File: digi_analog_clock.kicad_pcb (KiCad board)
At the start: 2 copper layers, 172 parts, among them SW1 SW_Push, SW2 SW_Push, U1 ATtiny13A-SSU, U2 MCP7940N-xSN, Y1 7pF CL

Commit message: Some updates, not finished
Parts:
- added J1: USB_B_Micro, digikey-footprints:USB_Micro_B_Female_10118194-0001LF, B.Cu at (100.0, 145.0)
- BT1, C1, C2, R3: moved to B.Cu
- moved D49 148.3 mm to (62.9, 87.9), turned to 162 degrees
- moved D50 143.9 mm to (64.4, 84.1), turned to 156 degrees
- moved D51 143.5 mm to (66.2, 80.5), turned to 150 degrees
- moved C13 137.7 mm to (65.8, 88.9), turned to 252 degrees
- moved D52 137.0 mm to (68.4, 77.1), turned to 144 degrees
- moved D53 135.9 mm to (71.0, 73.9), turned to 138 degrees
- moved D54 129.0 mm to (73.9, 71.0), turned to 132 degrees
- moved D129 126.9 mm to (61.0, 122.5), turned to 210 degrees
- moved D130 122.2 mm to (55.0, 100.0), turned to 180 degrees
- moved D96 122.1 mm to (83.5, 128.6), turned to 240 degrees
- moved D36 120.4 mm to (80.5, 133.8), turned to 240 degrees
- moved D95 117.2 mm to (86.6, 130.1), turned to 246 degrees
- moved D131 116.4 mm to (61.0, 77.5), turned to 150 degrees
- moved D128 116.1 mm to (77.5, 139.0), turned to 240 degrees
- moved D93 114.8 mm to (93.1, 132.3), turned to 258 degrees
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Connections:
- net /sheet5E4278E1/DIN renamed /6x_sk6805_1515_hours_1/DIN
- net /sheet5E4278E2/DIN renamed /6x_sk6805_1515_hours_2/DIN
- D1 pad 3: /6x_sk6805_1515_mins_2/DIN -> /6x_sk6805_1515_mins_1/DIN
- D12 pad 1: /6x_sk6805_1515_mins_4/DIN -> /6x_sk6805_1515_mins_3/DIN
- D13 pad 3: /6x_sk6805_1515_mins_4/DIN -> /6x_sk6805_1515_mins_3/DIN
- D132 pad 1: /sheet5E4278E2/DOUT -> (no net)
- D18 pad 1: /6x_sk6805_1515_mins_5/DIN -> /6x_sk6805_1515_mins_4/DIN
- D19 pad 3: /6x_sk6805_1515_mins_5/DIN -> /6x_sk6805_1515_mins_4/DIN
- D24 pad 1: /6x_sk6805_1515_mins_6/DIN -> /6x_sk6805_1515_mins_5/DIN
- D25 pad 3: /6x_sk6805_1515_mins_1/DIN -> /6x_sk6805_1515_mins_5/DIN
- D30 pad 1: /6x_sk6805_1515_mins_2/DIN -> /6x_sk6805_1515_mins_6/DIN
- D6 pad 1: /6x_sk6805_1515_mins_3/DIN -> /6x_sk6805_1515_mins_2/DIN
- D61 pad 3: /6x_sk6805_1515_secs_2/DIN -> /6x_sk6805_1515_secs_1/DIN
- D66 pad 1: /6x_sk6805_1515_secs_3/DIN -> /6x_sk6805_1515_secs_2/DIN
- D67 pad 3: /6x_sk6805_1515_secs_3/DIN -> /6x_sk6805_1515_secs_2/DIN
- D7 pad 3: /6x_sk6805_1515_mins_3/DIN -> /6x_sk6805_1515_mins_2/DIN
- D72 pad 1: /6x_sk6805_1515_secs_4/DIN -> /6x_sk6805_1515_secs_3/DIN
- D73 pad 3: /6x_sk6805_1515_secs_4/DIN -> /6x_sk6805_1515_secs_3/DIN
- D78 pad 1: /6x_sk6805_1515_secs_5/DIN -> /6x_sk6805_1515_secs_4/DIN
- D79 pad 3: /6x_sk6805_1515_secs_5/DIN -> /6x_sk6805_1515_secs_4/DIN
- D84 pad 1: /6x_sk6805_1515_secs_6/DIN -> /6x_sk6805_1515_secs_5/DIN
- D85 pad 3: /6x_sk6805_1515_secs_1/DIN -> /6x_sk6805_1515_secs_5/DIN
- D90 pad 1: /6x_sk6805_1515_secs_2/DIN -> /6x_sk6805_1515_secs_6/DIN
- U2 pad 7: Net-(U2-Pad7) -> (no net)
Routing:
- added copper zone on B.Cu, net GND
- added copper zone on F.Cu, net GND
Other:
- board outline added: 98 x 98 mm

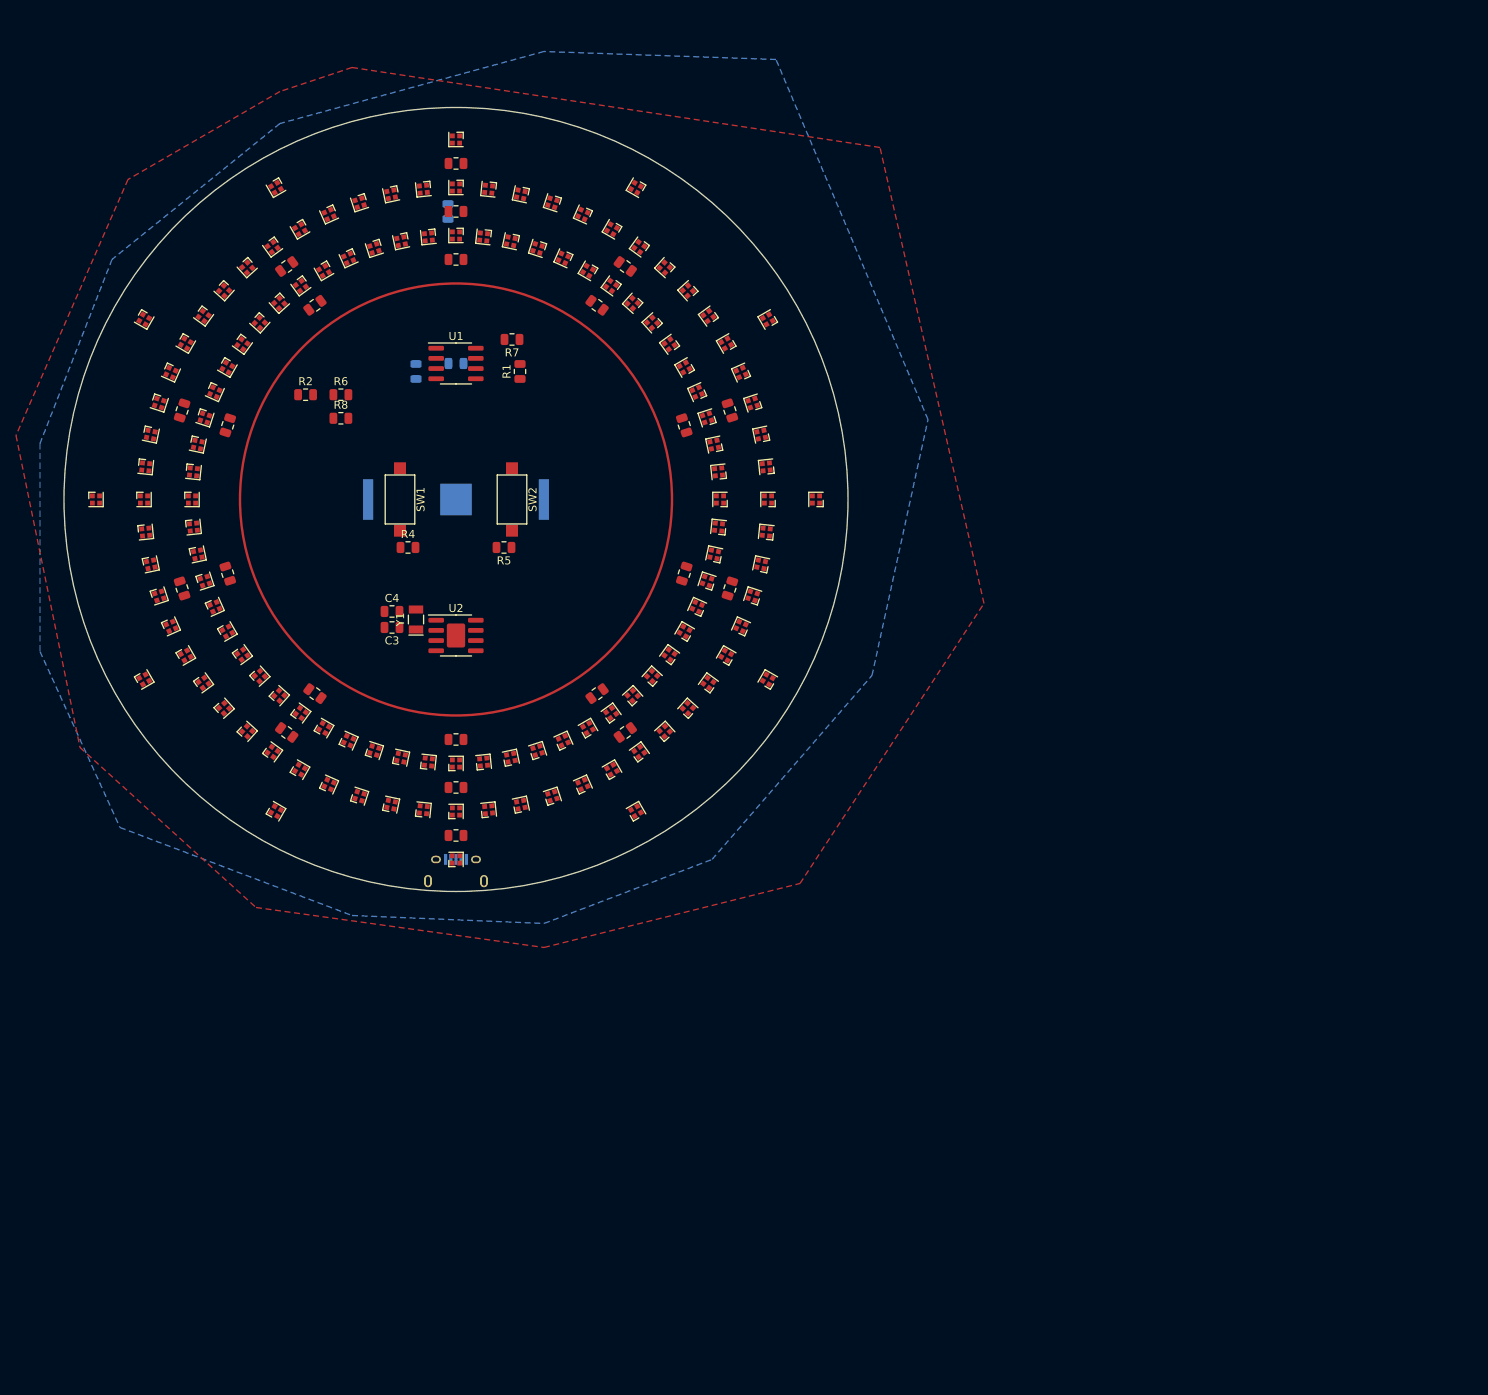
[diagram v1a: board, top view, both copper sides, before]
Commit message: Use atsamd21; do most layout
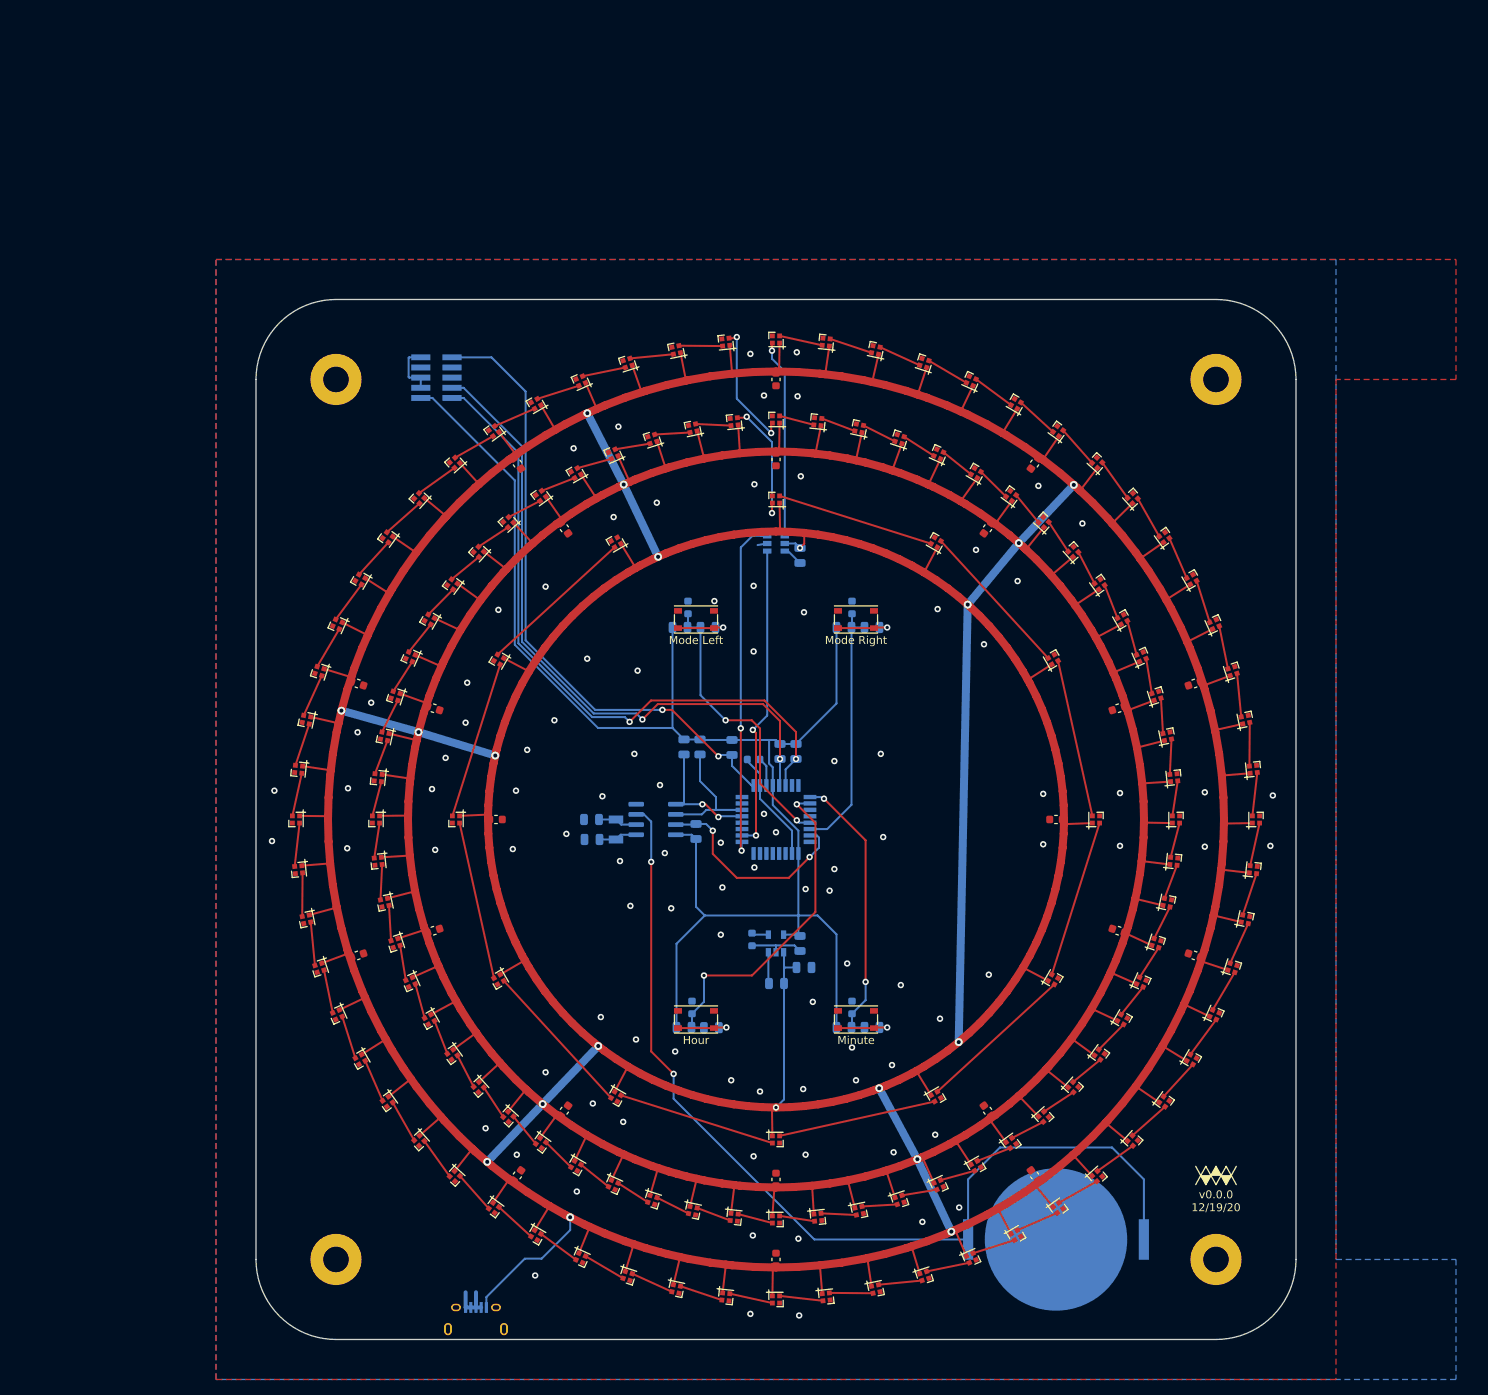
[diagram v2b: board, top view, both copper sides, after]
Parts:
- removed SW1, SW2: SW_Push, Button_Switch_SMD:SW_SPST_CK_RS282G05A3
- added C27: C, Capacitor_SMD:C_0603_1608Metric, F.Cu at (113.5, 176.4)
- added C28: C, Capacitor_SMD:C_0603_1608Metric, F.Cu at (97.2, 153.9)
- added C29: C, Capacitor_SMD:C_0603_1608Metric, F.Cu at (97.2, 126.1)
- added C30: C, Capacitor_SMD:C_0603_1608Metric, F.Cu at (113.5, 103.6)
- added C31: C, Capacitor_SMD:C_0603_1608Metric, F.Cu at (175.0, 140.0)
- added C32: C, Capacitor_SMD:C_0603_1608Metric, F.Cu at (105.0, 140.0)
- added Hour: SW_Push, WM_lib:SW_Push_1P1T_Vertical_CK_PTS815, F.Cu at (130.0, 165.0)
- added J2: Conn_ARM_JTAG_SWD_10, Connector_PinHeader_1.27mm:PinHeader_2x05_P1.27mm_Vertical_SMD, B.Cu at (97.5, 84.8)
- added Minute: SW_Push, WM_lib:SW_Push_1P1T_Vertical_CK_PTS815, F.Cu at (150.0, 165.0)
- added Mode Left: SW_Push, WM_lib:SW_Push_1P1T_Vertical_CK_PTS815, F.Cu at (130.0, 115.0)
- added Mode Right: SW_Push, WM_lib:SW_Push_1P1T_Vertical_CK_PTS815, F.Cu at (150.0, 115.0)
- added R10: 10kR, Resistor_SMD:R_0805_2012Metric, B.Cu at (148.5, 116.0)
- added R11: 1kR, Resistor_SMD:R_0805_2012Metric, B.Cu at (131.5, 116.0)
- added R12: 10kR, Resistor_SMD:R_0805_2012Metric, B.Cu at (128.0, 116.0)
- added R13: 1kR, Resistor_SMD:R_0805_2012Metric, B.Cu at (131.9, 166.0)
- added R14: 10kR, Resistor_SMD:R_0805_2012Metric, B.Cu at (128.5, 166.0)
- added R15: 1kR, Resistor_SMD:R_0805_2012Metric, B.Cu at (152.0, 166.0)
- added R16: 10kR, Resistor_SMD:R_0805_2012Metric, B.Cu at (148.5, 166.0)
- added R9: 1kR, Resistor_SMD:R_0805_2012Metric, B.Cu at (152.0, 116.0)
- added REF**: Logo_WM, Symbol:Logo_WM, F.Cu at (195.0, 184.5)
- added REF**: MountingHole_3.2mm_M3_Pad, MountingHole:MountingHole_3.2mm_M3_Pad, F.Cu at (85.0, 195.0)
- added REF**: MountingHole_3.2mm_M3_Pad, MountingHole:MountingHole_3.2mm_M3_Pad, F.Cu at (195.0, 195.0)
- added REF**: MountingHole_3.2mm_M3_Pad, MountingHole:MountingHole_3.2mm_M3_Pad, F.Cu at (195.0, 85.0)
- added REF**: MountingHole_3.2mm_M3_Pad, MountingHole:MountingHole_3.2mm_M3_Pad, F.Cu at (85.0, 85.0)
- added U3: ATSAMD21E15L-A, Package_QFP:TQFP-32_7x7mm_P0.8mm, B.Cu at (140.0, 140.0)
- added U4: ATtiny10-TS, Package_TO_SOT_SMD:SOT-23-6, B.Cu at (140.0, 105.5)
- C10, C5, C6, C7, C8, C9: value C -> 10kpF; footprint Capacitor_SMD:C_0805_2012Metric -> Capacitor_SMD:C_0603_1608Metric; moved to B.Cu
- C11, C12, C13, C14, C15, C16, C17, C18, C19, C20, C21, C22, C23, C24, C25, C26: footprint Capacitor_SMD:C_0805_2012Metric -> Capacitor_SMD:C_0603_1608Metric
- C3, C4, R1, R2, R4, R5, R6, R7, R8, Y1: moved to B.Cu
- R3: value 600R -> 10kR
- U1: value ATtiny13A-SSU -> MCP7940N-xSN; moved to B.Cu
- U2: value MCP7940N-xSN -> TC2014-3.3VxCTTR; footprint Package_SO:SOIC-8-1EP_3.9x4.9mm_P1.27mm_EP2.29x3mm -> Package_TO_SOT_SMD:SOT-23-5; moved to B.Cu
- moved C14 142.4 mm to (192.3, 157.0), turned to 162 degrees
- moved C25 135.8 mm to (166.5, 176.4), turned to 126 degrees
- moved C15 135.4 mm to (172.3, 184.5), turned to 126 degrees
- moved C13 131.1 mm to (192.3, 123.0), turned to 198 degrees
- moved C24 127.3 mm to (182.8, 153.9), turned to 162 degrees
- moved C16 121.3 mm to (140.0, 195.0), turned to 90 degrees
- moved BT1 119.1 mm to (175.0, 192.5)
- moved C23 116.8 mm to (182.8, 126.1), turned to 198 degrees
- moved C12 107.7 mm to (172.3, 95.5), turned to 234 degrees
- moved C5 98.2 mm to (137.0, 155.0), turned to 270 degrees
- moved C17 96.1 mm to (107.7, 184.5), turned to 54 degrees
- moved C22 95.2 mm to (166.5, 103.6), turned to 234 degrees
- moved R8 89.2 mm to (140.1, 160.5), turned to 180 degrees
- moved C1 87.1 mm to (143.5, 158.5), turned to 0 degrees
- moved C2 86.1 mm to (143.0, 155.5)
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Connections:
- net /6x_sk6805_1515_hours_1/DIN renamed HOURS
- net /6x_sk6805_1515_secs_1/DIN renamed MINUTES
- C1 pad 1: Net-(C1-Pad1) -> +5V
- C10 pad 1: +5V -> GND
- C10 pad 2: GND -> MM
- C2 pad 1: Net-(C2-Pad1) -> +3.3V
- C5 pad 1: +5V -> Net-(C5-Pad1)
- C6 pad 1: +5V -> GND
- C6 pad 2: GND -> Net-(C6-Pad2)
- C7 pad 1: +5V -> GND
- C7 pad 2: GND -> MODE2
- C8 pad 1: +5V -> GND
- C8 pad 2: GND -> MODE1
- C9 pad 1: +5V -> GND
- C9 pad 2: GND -> HH
- D1 pad 3: /6x_sk6805_1515_mins_1/DIN -> LED
- D102 pad 1: /6x_sk6805_1515_secs_8/DIN -> /6x_sk6805_1515_mins_8/DIN
- D103 pad 3: /6x_sk6805_1515_secs_8/DIN -> /6x_sk6805_1515_mins_8/DIN
- D108 pad 1: /6x_sk6805_1515_secs_9/DIN -> /6x_sk6805_1515_mins_9/DIN
- D109 pad 3: /6x_sk6805_1515_secs_9/DIN -> /6x_sk6805_1515_mins_9/DIN
- D114 pad 1: /6x_sk6805_1515_secs_10/DIN -> /6x_sk6805_1515_mins_10/DIN
- D115 pad 3: /6x_sk6805_1515_secs_10/DIN -> /6x_sk6805_1515_mins_10/DIN
- D12 pad 1: /6x_sk6805_1515_mins_3/DIN -> /6x_sk6805_1515_secs_3/DIN
- D13 pad 3: /6x_sk6805_1515_mins_3/DIN -> /6x_sk6805_1515_secs_3/DIN
- D18 pad 1: /6x_sk6805_1515_mins_4/DIN -> /6x_sk6805_1515_secs_4/DIN
- D19 pad 3: /6x_sk6805_1515_mins_4/DIN -> /6x_sk6805_1515_secs_4/DIN
- D24 pad 1: /6x_sk6805_1515_mins_5/DIN -> /6x_sk6805_1515_secs_5/DIN
- D25 pad 3: /6x_sk6805_1515_mins_5/DIN -> /6x_sk6805_1515_secs_5/DIN
- D30 pad 1: /6x_sk6805_1515_mins_6/DIN -> /6x_sk6805_1515_secs_6/DIN
- D31 pad 3: /6x_sk6805_1515_mins_6/DIN -> /6x_sk6805_1515_secs_6/DIN
- D36 pad 1: /6x_sk6805_1515_mins_7/DIN -> /6x_sk6805_1515_secs_7/DIN
- D37 pad 3: /6x_sk6805_1515_mins_7/DIN -> /6x_sk6805_1515_secs_7/DIN
- D42 pad 1: /6x_sk6805_1515_mins_8/DIN -> /6x_sk6805_1515_secs_8/DIN
- D43 pad 3: /6x_sk6805_1515_mins_8/DIN -> /6x_sk6805_1515_secs_8/DIN
- D48 pad 1: /6x_sk6805_1515_mins_9/DIN -> /6x_sk6805_1515_secs_9/DIN
- D49 pad 3: /6x_sk6805_1515_mins_9/DIN -> /6x_sk6805_1515_secs_9/DIN
- D54 pad 1: /6x_sk6805_1515_mins_10/DIN -> /6x_sk6805_1515_secs_10/DIN
- D55 pad 3: /6x_sk6805_1515_mins_10/DIN -> /6x_sk6805_1515_secs_10/DIN
- D6 pad 1: /6x_sk6805_1515_mins_2/DIN -> /6x_sk6805_1515_secs_2/DIN
- D66 pad 1: /6x_sk6805_1515_secs_2/DIN -> /6x_sk6805_1515_mins_2/DIN
- D67 pad 3: /6x_sk6805_1515_secs_2/DIN -> /6x_sk6805_1515_mins_2/DIN
- D7 pad 3: /6x_sk6805_1515_mins_2/DIN -> /6x_sk6805_1515_secs_2/DIN
- D72 pad 1: /6x_sk6805_1515_secs_3/DIN -> /6x_sk6805_1515_mins_3/DIN
- D73 pad 3: /6x_sk6805_1515_secs_3/DIN -> /6x_sk6805_1515_mins_3/DIN
- D78 pad 1: /6x_sk6805_1515_secs_4/DIN -> /6x_sk6805_1515_mins_4/DIN
- D79 pad 3: /6x_sk6805_1515_secs_4/DIN -> /6x_sk6805_1515_mins_4/DIN
- D84 pad 1: /6x_sk6805_1515_secs_5/DIN -> /6x_sk6805_1515_mins_5/DIN
- D85 pad 3: /6x_sk6805_1515_secs_5/DIN -> /6x_sk6805_1515_mins_5/DIN
- D90 pad 1: /6x_sk6805_1515_secs_6/DIN -> /6x_sk6805_1515_mins_6/DIN
- D91 pad 3: /6x_sk6805_1515_secs_6/DIN -> /6x_sk6805_1515_mins_6/DIN
- D96 pad 1: /6x_sk6805_1515_secs_7/DIN -> /6x_sk6805_1515_mins_7/DIN
- D97 pad 3: /6x_sk6805_1515_secs_7/DIN -> /6x_sk6805_1515_mins_7/DIN
- J1 pad 2: (no net) -> GND
- J1 pad 3: (no net) -> GND
- J1 pad 4: (no net) -> GND
- R1 pad 1: /SCL -> +3.3V
- R1 pad 2: +5V -> RESET3.3
- R2 pad 1: /SDA -> +3.3V
- R2 pad 2: +5V -> MFP
- R3 pad 1: /6x_sk6805_1515_mins_1/DIN -> +3.3V
- R3 pad 2: Net-(R3-Pad2) -> SCL
- R4 pad 1: Net-(R4-Pad1) -> +3.3V
- R4 pad 2: Net-(C1-Pad1) -> SDA
- R5 pad 1: Net-(R5-Pad1) -> +3.3V
- R5 pad 2: Net-(C2-Pad1) -> SWDCLK
- R6 pad 1: +5V -> +3.3V
- R6 pad 2: Net-(R6-Pad2) -> SWDIO
- R7 pad 2: Net-(C1-Pad1) -> RESET5
- R8 pad 2: Net-(C2-Pad1) -> Net-(R8-Pad2)
- U1 pad 1: Net-(R6-Pad2) -> Net-(C4-Pad2)
- U1 pad 2: Net-(C2-Pad1) -> Net-(C3-Pad1)
- U1 pad 3: Net-(R3-Pad2) -> Net-(BT1-Pad1)
- U1 pad 5: /SCL -> SDA
- U1 pad 6: /SDA -> SCL
- U1 pad 7: Net-(C1-Pad1) -> MFP
- U1 pad 8: +5V -> +3.3V
- U2 pad 1: Net-(C4-Pad2) -> +5V
- U2 pad 2: Net-(C3-Pad1) -> GND
- U2 pad 3: Net-(BT1-Pad1) -> Net-(R8-Pad2)
- U2 pad 4: GND -> Net-(C5-Pad1)
- U2 pad 5: /SDA -> +3.3V
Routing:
- net +5V: track 0.00 -> 1536.1 mm, vias 0 -> 19
- net +3.3V: track 0.00 -> 191.6 mm
- net Net-(BT1-Pad1): track 0.00 -> 122.4 mm, vias 0 -> 2
- net SWDIO: track 0.00 -> 83.7 mm, vias 0 -> 2
- net SWDCLK: track 0.00 -> 82.3 mm, vias 0 -> 2
- net RESET3.3: track 0.00 -> 79.0 mm, vias 0 -> 2
- net MOSI: track 0.00 -> 43.0 mm, vias 0 -> 2
- net HH: track 0.00 -> 42.0 mm, vias 0 -> 2
- net SCK: track 0.00 -> 38.2 mm, vias 0 -> 2
- net MODE1: track 0.00 -> 36.1 mm, vias 0 -> 2
- net GND: track 0.00 -> 35.0 mm, vias 0 -> 98
- net MM: track 0.00 -> 34.9 mm, vias 0 -> 2
- net MODE2: track 0.00 -> 32.0 mm
- net MFP: track 0.00 -> 26.5 mm, vias 0 -> 2
- net LED: track 0.00 -> 24.8 mm, vias 0 -> 1
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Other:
- board size 98 x 98 mm -> 130 x 130 mm
- rule pad_to_mask_clearance: 0.051 -> 0.05
- board text added: "v0.0.0 12/19/20"

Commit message: Add yggdrasil art; plot
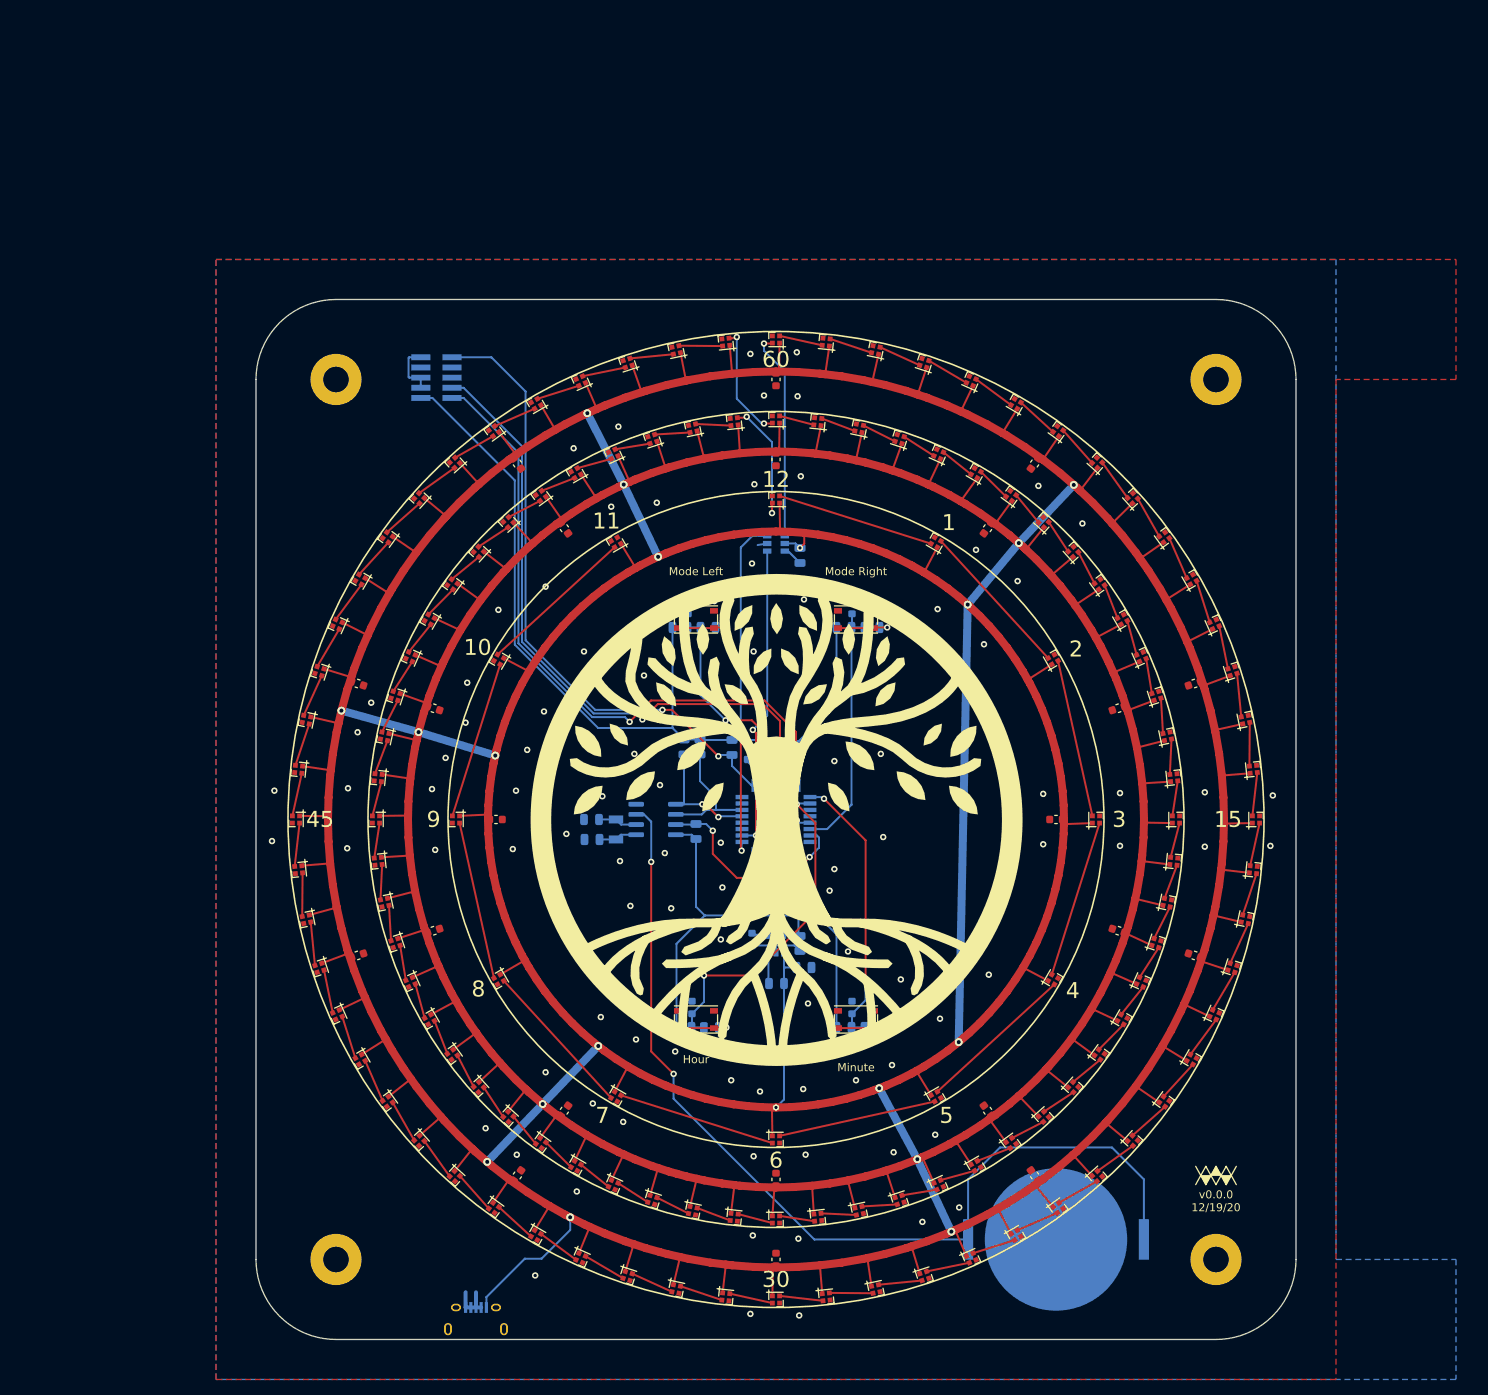
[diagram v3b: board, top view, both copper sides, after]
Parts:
- added REF**: logo_yggdrasil, WM_lib:yggdrasil, F.Cu at (140.0, 140.0)
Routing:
- net MINUTES: track 16.1 -> 14.5 mm
- net LED: track 24.8 -> 26.2 mm
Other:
- board text added: "1"
- board text added: "10"
- board text added: "11"
- board text added: "12"
- board text added: "15"
- board text added: "2"
- board text added: "3"
- board text added: "30"
- board text added: "4"
- board text added: "45"
- board text added: "5"
- board text added: "6"
- board text added: "60"
- board text added: "7"
- board text added: "8"
- board text added: "9"
